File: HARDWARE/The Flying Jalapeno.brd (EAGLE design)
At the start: 73.7 x 72.4 mm, 97 parts, among them Q2 MMBT2222A, Q3 NDP6020P, Q4 MMBT2222A, Q5 NDP6020P, Q6 BSS138, 200mA/50V, Q7 BSS138, 200mA/50V, U1 ATMEGA2560AU, U2 LM1117, U3 LM1117, U4 LM1117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

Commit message: incremented version number to v10
in sch and brd
Had to nudge traces around when I replaced the fj connector for the
updated package.
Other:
- board text added: "V10"
- board text removed: "V02"
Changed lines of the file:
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@@
 <text x="51.054" y="58.801" size="0.8128" layer="21" font="vector" ratio="15" rot="R90">BLK</text>
 <text x="66.548" y="58.801" size="0.8128" layer="21" font="vector" ratio="15" rot="R90">GRN</text>
-<text x="40.64" y="69.85" size="1.27" layer="16" font="vector" ratio="15" rot="MR0">V02</text>
+<text x="40.64" y="69.85" size="1.27" layer="16" font="vector" ratio="15" rot="MR0">V10</text>
 <text x="7.239" y="70.231" size="1.27" layer="21" font="vector" ratio="15">VOLTAGE</text>
 <text x="2.2352" y="43.7388" size="0.6096" layer="21" font="vector" ratio="15" rot="R270">RAW</text>

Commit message: update red leds to correct part/prod_ids
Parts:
- renumbered Q7 to Q1
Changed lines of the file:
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@@
 <attribute name="NAME" x="56.007" y="16.5674" size="1.27" layer="25" rot="R270"/>
 <attribute name="VALUE" value="RED" x="56.6674" y="19.3162" size="0.4064" layer="27" rot="R270"/>
-<attribute name="PROD_ID" value="DIO-00809" x="56.007" y="18.5674" size="1.778" layer="27" display="off"/>
+<attribute name="PROD_ID" value="DIO-09912" x="56.007" y="18.5674" size="1.778" layer="27" display="off"/>
 </element>
 <element name="Y1" library="SparkFun-FreqCtrl" package="RESONATOR-SMD" value="16MHZ" x="58.16695" y="23.906809375" smashed="yes" rot="R225">
@@
 </element>
 <element name="D1" library="SparkFun-LED" package="LED-1206" value="RED" x="7.8232" y="35.8267">
-<attribute name="PROD_ID" value="DIO-00809" x="7.8232" y="35.8267" size="1.778" layer="27" display="off"/>
+<attribute name="PROD_ID" value="DIO-09912" x="7.8232" y="35.8267" size="1.778" layer="27" display="off"/>
 <attribute name="VALUE" value="RED" x="7.8232" y="35.8267" size="1.778" layer="27" display="off"/>
 </element>
@@
 </element>
 <element name="D4" library="SparkFun-LED" package="LED-1206" value="RED" x="19.6596" y="35.687">
-<attribute name="PROD_ID" value="DIO-00809" x="19.6596" y="35.687" size="1.778" layer="27" display="off"/>
+<attribute name="PROD_ID" value="DIO-09912" x="19.6596" y="35.687" size="1.778" layer="27" display="off"/>
 <attribute name="VALUE" value="RED" x="19.6596" y="35.687" size="1.778" layer="27" display="off"/>
 </element>
@@
 </element>
 <element name="D6" library="SparkFun-LED" package="LED-1206" value="RED" x="27.94" y="68.58">
-<attribute name="PROD_ID" value="DIO-00809" x="27.94" y="68.58" size="1.778" layer="27" font="vector" ratio="15" display="off"/>
+<attribute name="PROD_ID" value="DIO-09912" x="27.94" y="68.58" size="1.778" layer="27" font="vector" ratio="15" display="off"/>
 </element>
 <element name="R31" library="SparkFun-Resistors" package="0603" value="1k" x="27.94" y="64.77" rot="R90">
@@
 <attribute name="VALUE" value="200mA/50V" x="61.7347" y="54.0131" size="1.778" layer="27" rot="R90" display="off"/>
 </element>
-<element name="Q7" library="SparkFun-DiscreteSemi" package="SOT23-3" value="BSS138, 200mA/50V" x="56.1467" y="53.8607" rot="R90">
+<element name="Q1" library="SparkFun-DiscreteSemi" package="SOT23-3" value="BSS138, 200mA/50V" x="56.1467" y="53.8607" rot="R90">
 <attribute name="PROD_ID" value="TRANS-00830" x="56.1467" y="53.8607" size="1.778" layer="27" rot="R90" display="off"/>
 <attribute name="VALUE" value="200mA/50V" x="56.1467" y="53.8607" size="1.778" layer="27" rot="R90" display="off"/>
@@
 <signal name="RX0">
 <contactref element="U1" pad="2"/>
-<contactref element="Q7" pad="3"/>
+<contactref element="Q1" pad="3"/>
 <contactref element="R33" pad="1"/>
 <wire x1="55.0467" y1="53.8607" x2="55.0467" y2="51.1008" width="0.3048" layer="1"/>
@@
 <signal name="FTDI_VCC">
 <contactref element="Q6" pad="1"/>
-<contactref element="Q7" pad="1"/>
+<contactref element="Q1" pad="1"/>
 <contactref element="R37" pad="2"/>
 <contactref element="R32" pad="2"/>
@@
 </signal>
 <signal name="N$16">
-<contactref element="Q7" pad="2"/>
+<contactref element="Q1" pad="2"/>
 <contactref element="R32" pad="1"/>
 <wire x1="58.5851" y1="54.6726" x2="57.2848" y2="54.6726" width="0.3048" layer="1"/>

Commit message: removed a small rouge trace off of RAW, must have been from v01
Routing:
- net RAW: track 155.5 -> 153.3 mm
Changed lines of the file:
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@@
 <layer number="14" name="Route14" color="1" fill="6" visible="no" active="no"/>
 <layer number="15" name="Route15" color="4" fill="6" visible="no" active="no"/>
-<layer number="16" name="Bottom" color="1" fill="1" visible="yes" active="yes"/>
+<layer number="16" name="Bottom" color="1" fill="1" visible="no" active="yes"/>
 <layer number="17" name="Pads" color="2" fill="1" visible="yes" active="yes"/>
 <layer number="18" name="Vias" color="2" fill="1" visible="yes" active="yes"/>
-<layer number="19" name="Unrouted" color="6" fill="1" visible="yes" active="yes"/>
+<layer number="19" name="Unrouted" color="6" fill="1" visible="no" active="yes"/>
 <layer number="20" name="Dimension" color="15" fill="1" visible="yes" active="yes"/>
-<layer number="21" name="tPlace" color="16" fill="1" visible="yes" active="yes"/>
-<layer number="22" name="bPlace" color="14" fill="1" visible="yes" active="yes"/>
-<layer number="23" name="tOrigins" color="15" fill="1" visible="yes" active="yes"/>
-<layer number="24" name="bOrigins" color="15" fill="1" visible="yes" active="yes"/>
+<layer number="21" name="tPlace" color="16" fill="1" visible="no" active="yes"/>
+<layer number="22" name="bPlace" color="14" fill="1" visible="no" active="yes"/>
+<layer number="23" name="tOrigins" color="15" fill="1" visible="no" active="yes"/>
+<layer number="24" name="bOrigins" color="15" fill="1" visible="no" active="yes"/>
 <layer number="25" name="tNames" color="7" fill="1" visible="no" active="yes"/>
 <layer number="26" name="bNames" color="7" fill="1" visible="no" active="yes"/>
@@
 <layer number="43" name="vRestrict" color="2" fill="10" visible="no" active="yes"/>
 <layer number="44" name="Drills" color="7" fill="1" visible="no" active="yes"/>
-<layer number="45" name="Holes" color="7" fill="1" visible="yes" active="yes"/>
+<layer number="45" name="Holes" color="7" fill="1" visible="no" active="yes"/>
 <layer number="46" name="Milling" color="3" fill="1" visible="no" active="yes"/>
 <layer number="47" name="Measures" color="7" fill="1" visible="no" active="yes"/>
 <layer number="48" name="Document" color="7" fill="1" visible="no" active="yes"/>
-<layer number="49" name="Reference" color="13" fill="1" visible="yes" active="yes"/>
+<layer number="49" name="Reference" color="13" fill="1" visible="no" active="yes"/>
 <layer number="50" name="dxf" color="7" fill="1" visible="no" active="yes"/>
-<layer number="51" name="tDocu" color="6" fill="1" visible="yes" active="yes"/>
+<layer number="51" name="tDocu" color="6" fill="1" visible="no" active="yes"/>
 <layer number="52" name="bDocu" color="7" fill="1" visible="no" active="yes"/>
 <layer number="53" name="tGND_GNDA" color="7" fill="9" visible="no" active="no"/>
@@
 <wire x1="19.7261" y1="56.1848" x2="20.2819" y2="56.1848" width="1.016" layer="1"/>
 <wire x1="20.2819" y1="56.1848" x2="26.2509" y2="62.1538" width="1.016" layer="1"/>
-<wire x1="26.2509" y1="62.1538" x2="32.258" y2="62.1538" width="1.016" layer="1"/>
-<wire x1="32.258" y1="62.1538" x2="33.7693" y2="62.1538" width="1.016" layer="1"/>
+<wire x1="26.2509" y1="62.1538" x2="33.7693" y2="62.1538" width="1.016" layer="1"/>
 <wire x1="33.7693" y1="62.1538" x2="34.4424" y2="62.8269" width="1.016" layer="1"/>
 <wire x1="34.4424" y1="62.8269" x2="34.4424" y2="66.167" width="1.016" layer="1"/>
@@
 <via x="16.0909" y="52.7304" extent="1-16" drill="0.508"/>
 <wire x1="16.0909" y1="52.7304" x2="19.6342" y2="52.7304" width="1.016" layer="1"/>
-<wire x1="32.297" y1="59.9558" x2="32.258" y2="62.1538" width="0.3048" layer="1"/>
 <wire x1="3.8354" y1="45.5676" x2="3.8354" y2="44.2468" width="1.016" layer="1"/>
 <wire x1="3.8354" y1="44.2468" x2="3.8354" y2="42.9768" width="0.6096" layer="1"/>

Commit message: small nudges to some traces to get nicer angles and removes some unnecessary kinks
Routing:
- net TX1: track 43.6 -> 42.2 mm
- net RX1: track 45.7 -> 44.6 mm
- net 49/PWR_CTRL2: track 38.5 -> 37.6 mm
- net PB3: track 92.2 -> 91.5 mm
- net 48/PWR_CTRL1: track 54.6 -> 54.1 mm

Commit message: Fixed bPlace silk labels on 2x30 header
These used to overlap onto the pth headers cutting a lot of the silk.

This fixes issue #7

Also nudged some vias and traces to ensure none of the silk gets cut.

Also bumped silk up to 0.032, 18% (previously was 0.026). This should
look really nice on the next round of pcbs.
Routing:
- net PB0: track 48.6 -> 47.1 mm
- net 46/CAPSENSE2: track 38.5 -> 39.3 mm
- net D13: track 29.1 -> 29.8 mm
- net D12: track 21.2 -> 21.9 mm
- net 41/PASS: track 78.6 -> 79.3 mm
- net 40/FAIL: track 81.6 -> 82.3 mm
- net D11: track 27.5 -> 28.1 mm
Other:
- board text removed: "GNd"

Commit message: changed version to v11, to keep things straight.
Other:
- board text added: "V11"
- board text removed: "V10"
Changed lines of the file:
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@@
 <layer number="47" name="Measures" color="7" fill="1" visible="no" active="yes"/>
 <layer number="48" name="Document" color="7" fill="1" visible="no" active="yes"/>
-<layer number="49" name="Reference" color="13" fill="1" visible="yes" active="yes"/>
+<layer number="49" name="Reference" color="13" fill="1" visible="no" active="yes"/>
 <layer number="50" name="dxf" color="7" fill="1" visible="no" active="yes"/>
 <layer number="51" name="tDocu" color="6" fill="1" visible="yes" active="yes"/>
@@
 <text x="51.054" y="58.801" size="0.8128" layer="21" font="vector" ratio="15" rot="R90">BLK</text>
 <text x="66.548" y="58.801" size="0.8128" layer="21" font="vector" ratio="15" rot="R90">GRN</text>
-<text x="40.64" y="69.85" size="1.27" layer="16" font="vector" ratio="15" rot="MR0">V10</text>
+<text x="40.64" y="69.85" size="1.27" layer="16" font="vector" ratio="15" rot="MR0">V11</text>
 <text x="7.239" y="70.231" size="1.27" layer="21" font="vector" ratio="15">VOLTAGE</text>
 <text x="2.2352" y="43.7388" size="0.6096" layer="21" font="vector" ratio="15" rot="R270">RAW</text>

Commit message: cleaning up net naming convention on 48/49
"48/PWR_CTRL_V1" and "49/PWR_CTRL_V2".

issue #3
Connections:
- net 48/PWR_CTRL1 renamed 48/PWR_CTRL_1
- net 49/PWR_CTRL2 renamed 49/PWR_CTRL_2
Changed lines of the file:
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@@
 <wire x1="26.1992" y1="15.5956" x2="36.8554" y2="15.5956" width="0.3048" layer="1"/>
 </signal>
-<signal name="48/PWR_CTRL1">
+<signal name="48/PWR_CTRL_1">
 <contactref element="U1" pad="36"/>
 <contactref element="R11" pad="1"/>
@@
 <wire x1="23.9522" y1="40.9448" x2="28.2702" y2="36.6268" width="0.3048" layer="1"/>
 </signal>
-<signal name="49/PWR_CTRL2">
+<signal name="49/PWR_CTRL_2">
 <contactref element="U1" pad="35"/>
 <contactref element="R14" pad="1"/>

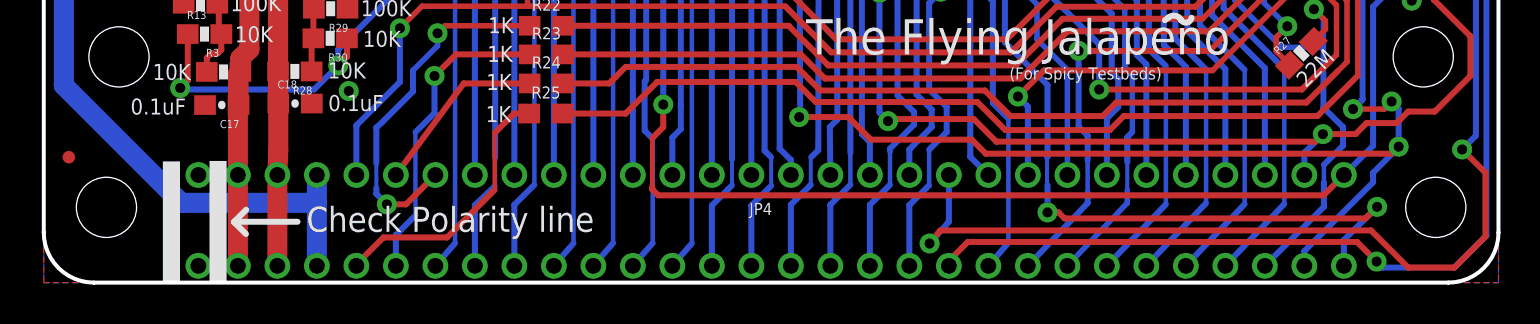
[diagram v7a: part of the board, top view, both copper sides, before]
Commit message: Updated FJ device - symbol and package
Symbol pins are now correctly named A0 and A1, they used to have A0/TX0
and A1/RX0, which is incorrect and left over from the mega pro designs.

Also, with this update to the device came a small update to the package.
Only thing effected was the drill hits for the brackets are now the
correct "tighter" size of 0.11".
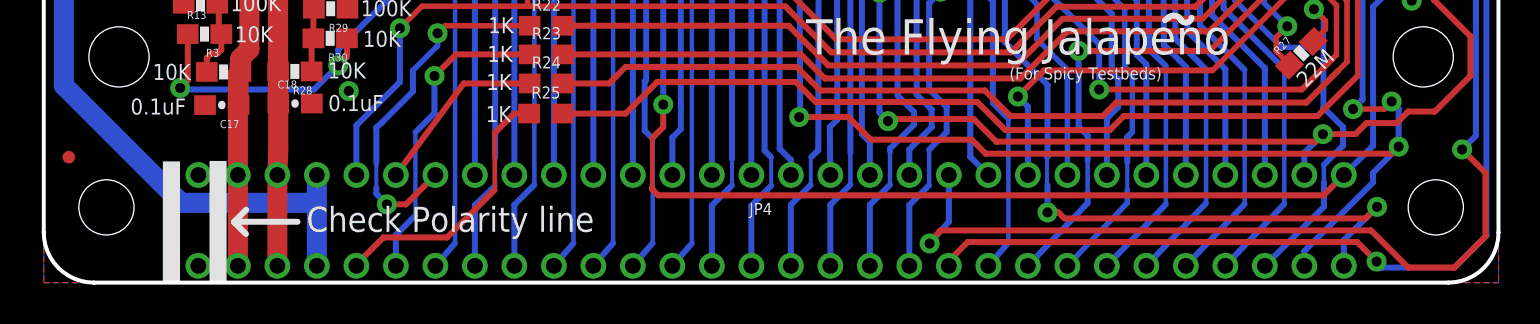
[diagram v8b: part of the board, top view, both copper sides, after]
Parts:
- JP4: device Testing:FLYING_JALAPENO_V2_F -> Testing:FLYING_JALAPENO_V3_F
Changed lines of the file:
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@@
 <attribute name="PROD_ID" value="CONN-08971" x="58.42" y="64.77" size="1.778" layer="27" rot="R180" display="off"/>
 </element>
-<element name="JP4" library="Testing" package="FLYING_JALAPENO_V2_F" value="2x30 RA FEMALE HEADER" x="36.83" y="0">
+<element name="JP4" library="Testing" package="FLYING_JALAPENO_V3_F" value="2x30 RA FEMALE HEADER" x="36.83" y="0">
 <attribute name="PROD_ID" value="CONN-13106" x="36.83" y="0" size="1.778" layer="27" display="off"/>
 </element>
